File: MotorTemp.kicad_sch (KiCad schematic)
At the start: 22 parts, among them U56 LMV321, U57 LMV321

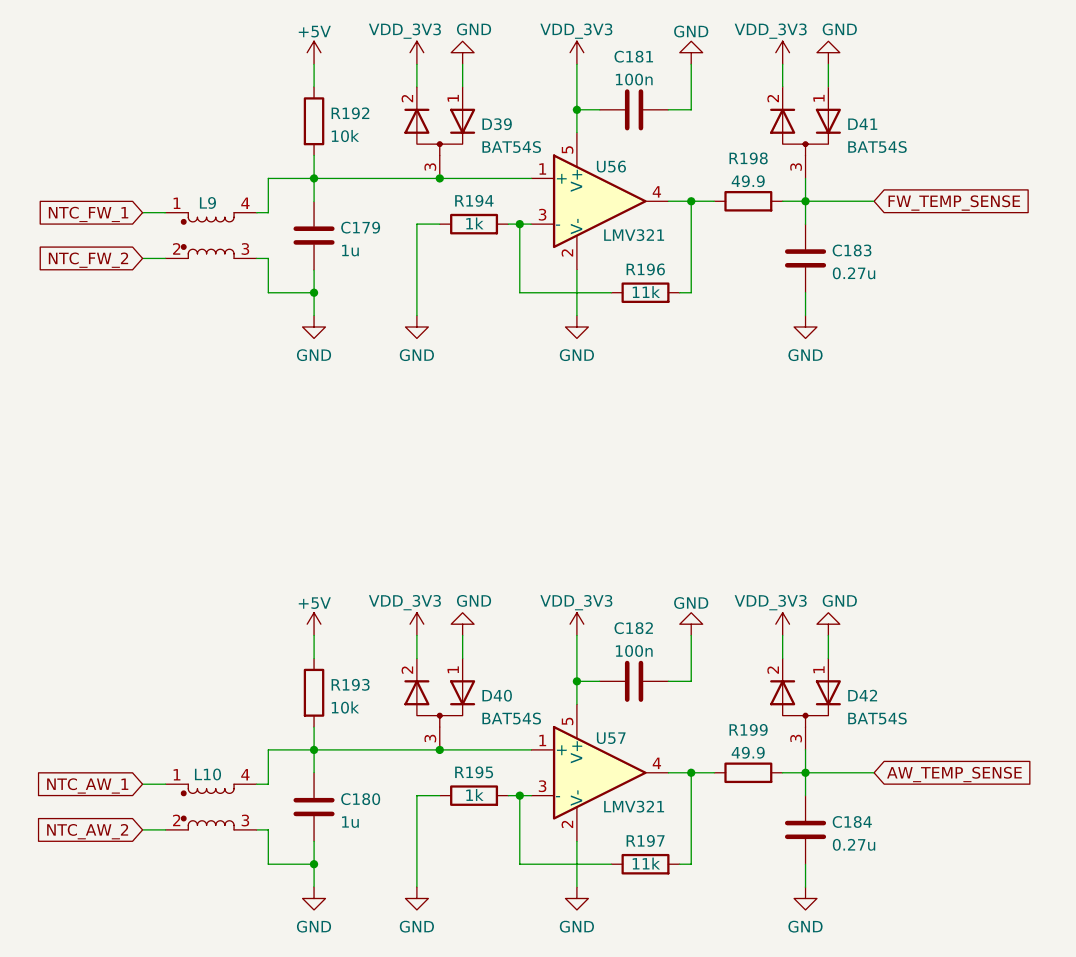
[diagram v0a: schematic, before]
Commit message: Изменения в схеме: убрал разъемы датчиков тока
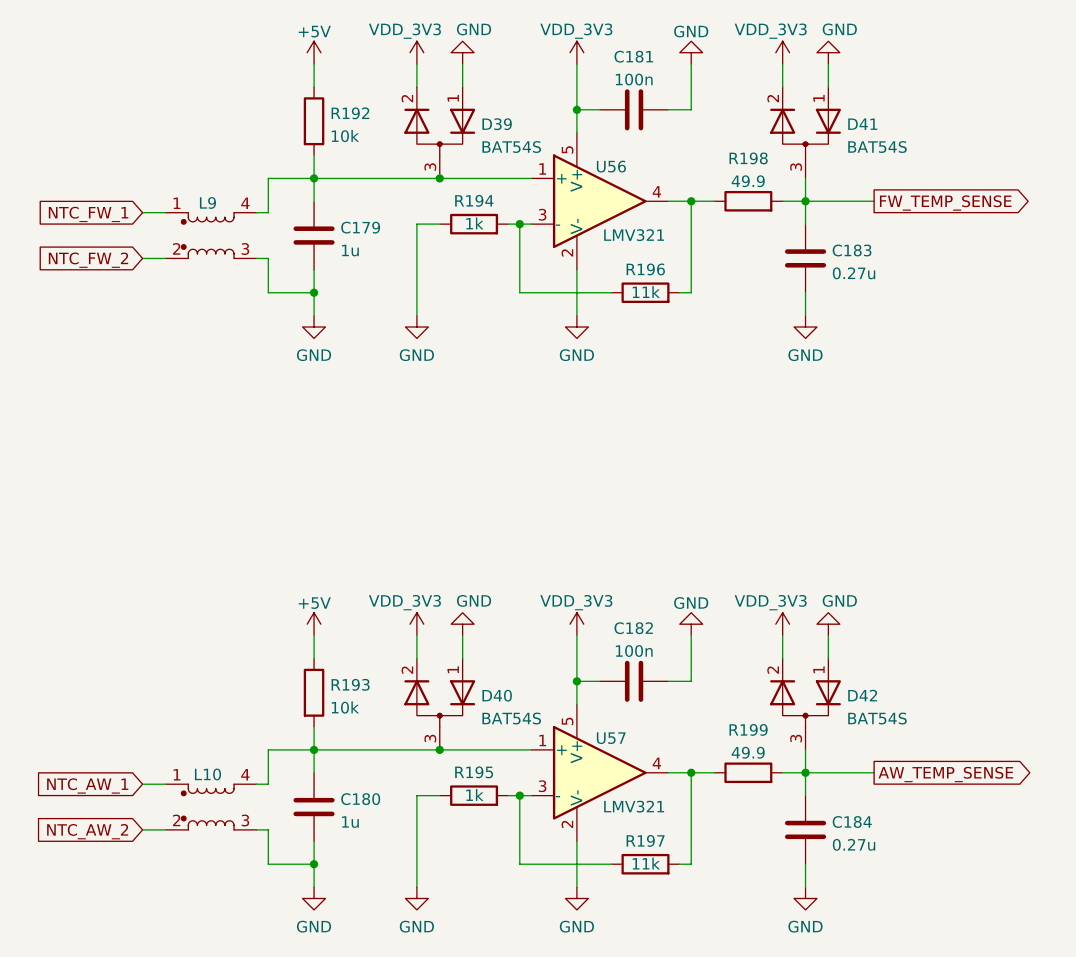
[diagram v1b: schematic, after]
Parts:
- L10, L9: value DR331-513AE -> DR331-513AE

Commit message: REV_C: добавил Э3
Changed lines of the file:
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@@
 (kicad_sch
-	(version 20231120)
+	(version 20250114)
 	(generator "eeschema")
-	(generator_version "8.0")
+	(generator_version "9.0")
 	(paper "A4")
+	(title_block
+		(comment 1 "НВЦТ.EVP150-2-1.3000.100 Э3")
+	)
 	(junction
 		(at 114.3 67.31)
